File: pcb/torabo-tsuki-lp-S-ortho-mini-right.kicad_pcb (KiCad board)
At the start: 2 copper layers, 123.8 x 71.8 mm, 50 parts, among them J201 Conn_01x06_MountingPin, SW201 SW_SPDT, SW44 SW_Push, SW45 SW_Push, SW46 SW_Push, SW47 SW_Push, SW48 SW_Push, SW51 SW_Push, SW52 SW_Push, SW53 SW_Push, SW54 SW_Push, SW55 SW_Push, SW58 SW_Push, SW59 SW_Push, SW60 SW_Push, SW61 SW_Push, SW62 SW_Push, SW63 SW_Push, SW65 SW_Push, SW69 SW_Push, SW70 SW_Push, U201 BLEMicroPro

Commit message: Add outer key columns to split PCBs
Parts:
- added D43: D_Small, Library:D_SOD-123_HandSoldering, B.Cu at (157.3, 122.1)
- added D50: D_Small, Library:D_SOD-123_HandSoldering, B.Cu at (157.3, 139.1)
- added D57: D_Small, Library:D_SOD-123_HandSoldering, B.Cu at (157.3, 156.1)
- added D64: D_Small, Library:D_SOD-123_HandSoldering, B.Cu at (157.3, 173.1)
- added SW43: SW_Push, Library:CHOC_V2_SOCKET_HANDSOLDERING_17mm, B.Cu at (155.8, 126.0)
- added SW50: SW_Push, Library:CHOC_V2_SOCKET_HANDSOLDERING_17mm, B.Cu at (155.8, 143.0)
- added SW57: SW_Push, Library:CHOC_V2_SOCKET_HANDSOLDERING_17mm, B.Cu at (155.8, 160.0)
- added SW64: SW_Push, Library:CHOC_V2_SOCKET_HANDSOLDERING_17mm, B.Cu at (155.8, 177.0)
- moved REF** 17.0 mm to (164.3, 186.5)
- moved REF** 17.0 mm to (164.3, 116.5)
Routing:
- net /right/COL0: track 0.00 -> 169.3 mm, vias 0 -> 2
- net /right/ROW4: track 134.6 -> 153.2 mm, vias 4 -> 5
- net /right/ROW2: track 86.5 -> 105.1 mm, vias 5 -> 6
- net /right/ROW3: track 116.3 -> 134.9 mm, vias 6 -> 7
- net /right/ROW1: track 92.7 -> 111.3 mm, vias 5 -> 6
- net Net-(D43-K): track 0.00 -> 9.80 mm
- net Net-(D64-K): track 0.00 -> 9.80 mm
- net Net-(D57-K): track 0.00 -> 9.80 mm
- net Net-(D50-K): track 0.00 -> 9.80 mm
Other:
- board size 123.8 x 71.8 mm -> 140.8 x 71.8 mm

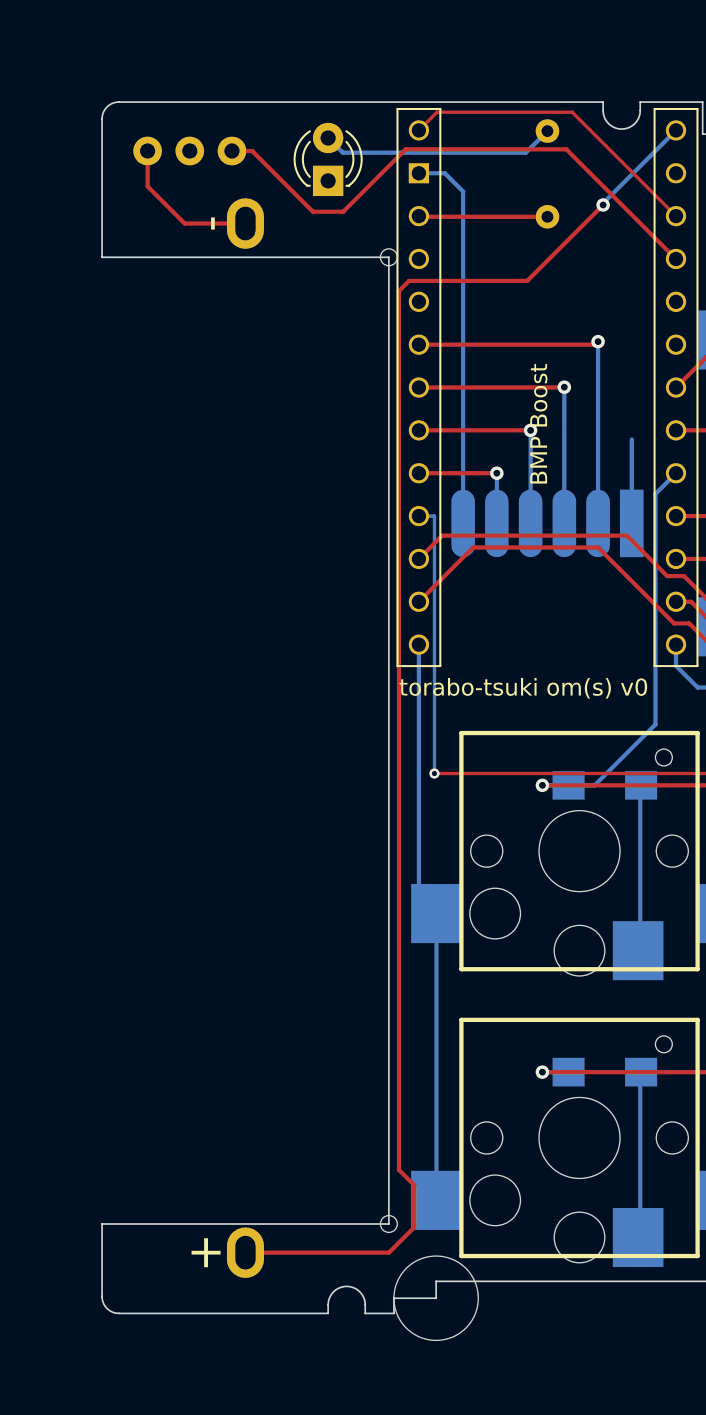
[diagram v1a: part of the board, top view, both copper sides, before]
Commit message: Adapt split keyboard PCBs for AAA battery holders
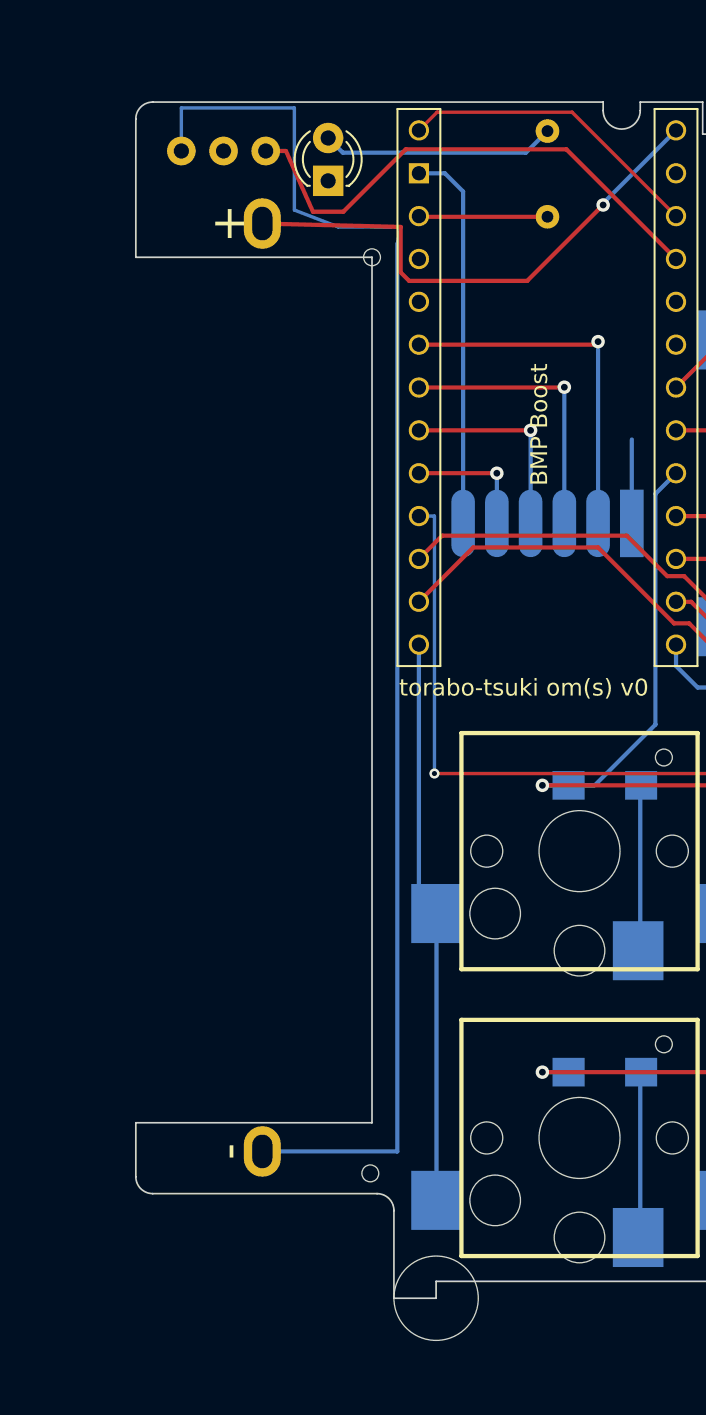
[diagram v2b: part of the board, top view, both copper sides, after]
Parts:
- BT201: value Battery_Cell -> Battery_Cell_AAA; footprint Library:battery_holder -> Library:battery_holder_AAA_1x_P55mm
- moved REF** 3.20 mm to (41.4, 179.1)
- moved BT201 3.16 mm to (35.0, 150.3), turned to 90 degrees
- moved SW201 2.00 mm to (32.7, 118.5)
- moved REF** 1.00 mm to (41.5, 124.8)
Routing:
- net Net-(BT201--): track 8.81 -> 84.6 mm
- net +BATT: track 86.9 -> 31.2 mm
- net /right/BOOT: track 32.0 -> 30.9 mm
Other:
- board size 140.8 x 71.8 mm -> 138.8 x 70.9 mm

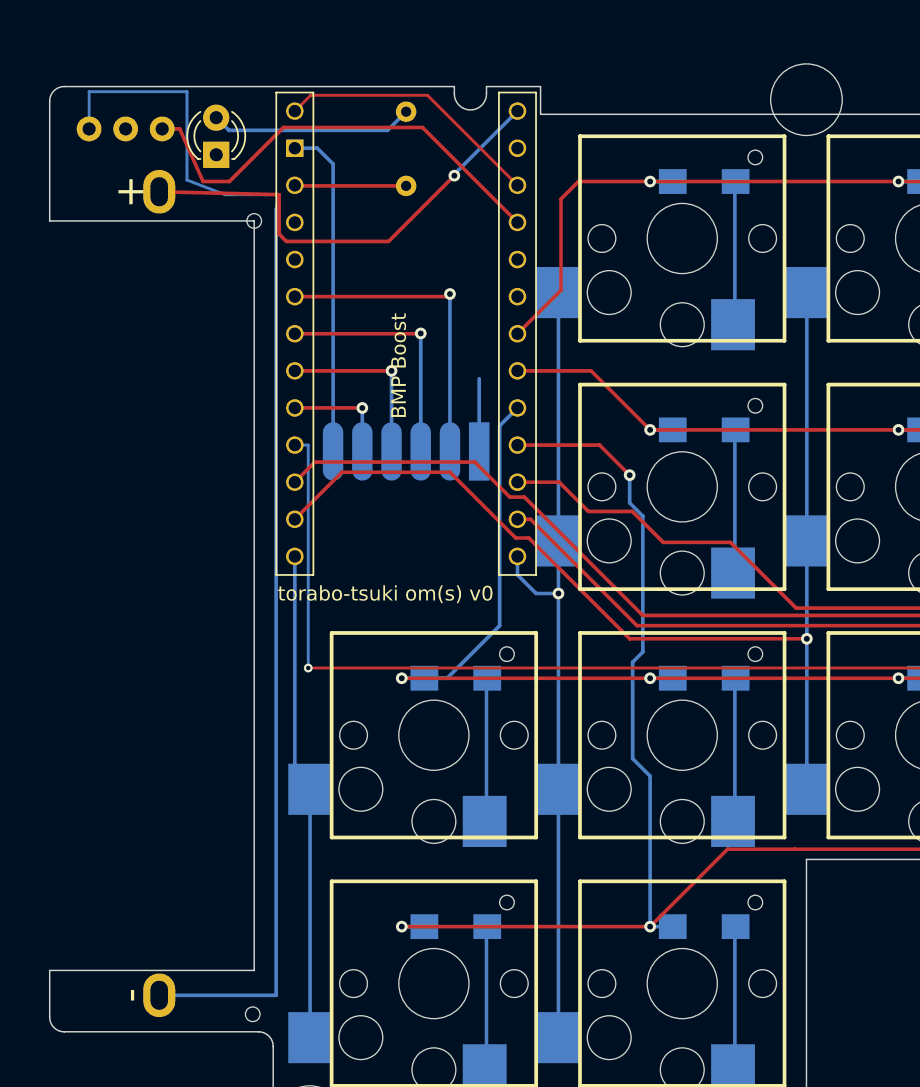
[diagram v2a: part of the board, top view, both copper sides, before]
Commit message: Migrate split PCBs to XIAO nRF52840 Plus
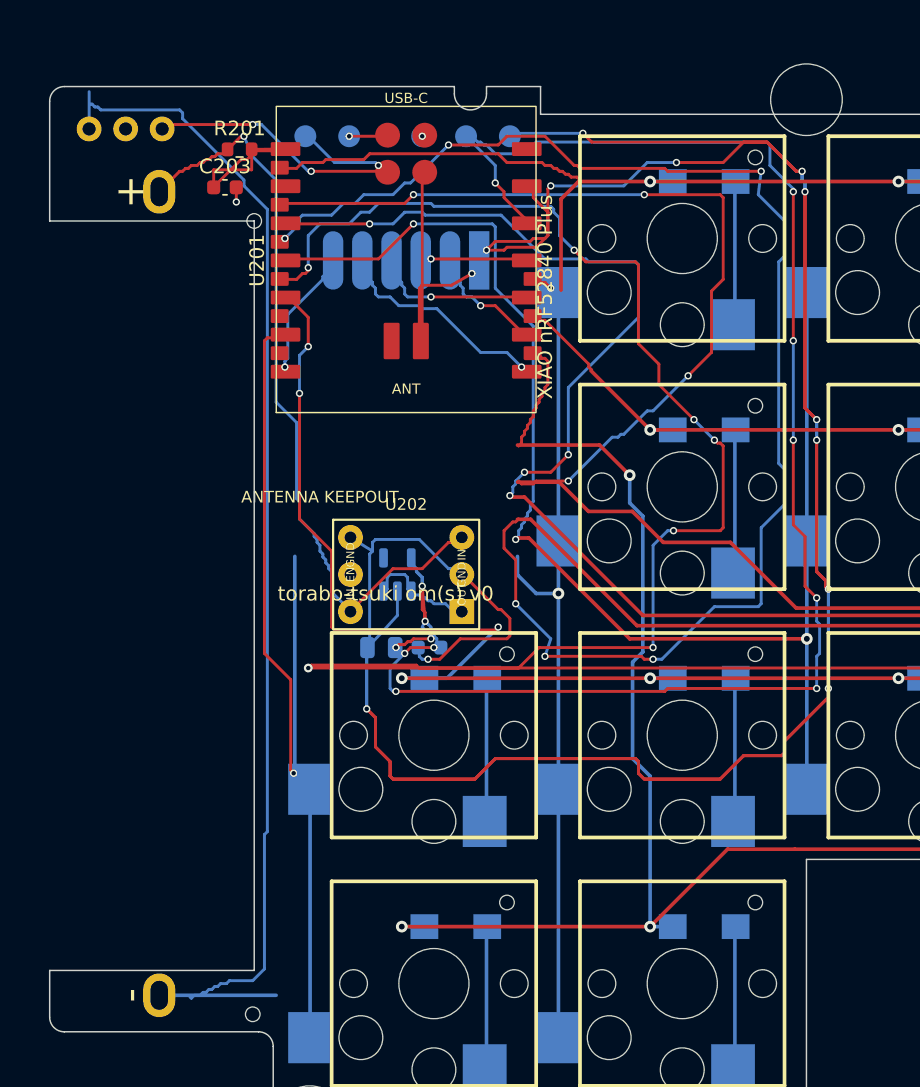
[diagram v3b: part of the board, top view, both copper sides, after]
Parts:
- removed D201: LED_Small, Library:LED_D3.0mm
- added C201: 10uF X7R, C_0805_2012Metric, B.Cu at (50.2, 154.0)
- added C202: 0.1uF X7R, C_0603_1608Metric, B.Cu at (53.5, 154.0)
- added C203: 0.1uF X7R, C_0603_1608Metric, F.Cu at (39.5, 122.5)
- added TP201: SWDIO, TestPoint_Pad_D1.5mm, B.Cu at (48.0, 119.0)
- added TP202: SWDCLK, TestPoint_Pad_D1.5mm, B.Cu at (53.0, 119.0)
- added TP203: RESET, TestPoint_Pad_D1.5mm, B.Cu at (45.0, 119.0)
- added TP204: 3V3, TestPoint_Pad_D1.5mm, B.Cu at (56.0, 119.0)
- added TP205: GND, TestPoint_Pad_D1.5mm, B.Cu at (59.0, 119.0)
- added U202: AE-XCL103-3V3, AE-XCL103-3V3, F.Cu at (51.9, 149.0)
- added U203: XC8111AA01MR-G, SOT-23-5, B.Cu at (51.3, 149.0)
- R201: value 330 -> 10k; footprint Library:R_Axial_DIN0204_L3.6mm_D1.6mm_P5.08mm_Horizontal -> R_0603_1608Metric; moved to F.Cu
- U201: value BLEMicroPro -> XIAO nRF52840 Plus; footprint Library:BLEMicroPro -> XIAO-nRF52840-Plus-SMD
- moved J201 13.1 mm to (51.9, 127.5)
- moved R201 11.7 mm to (40.5, 119.9), turned to 0 degrees
- moved U201 10.2 mm to (51.9, 127.5), turned to 90 degrees
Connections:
- R201 pad 1: /right/LED -> +BATT
- R201 pad 2: Net-(D201-A) -> /right/VBAT_ADC
- SW201 pad 3: /right/BOOT -> /right/RESET_N
- U201 pad 1: GND -> /right/VBAT_ADC
- U201 pad 10: /right/COL0 -> /right/MOTION
- U201 pad 11: /right/COL2 -> /right/SDIO
- U201 pad 12: /right/COL4 -> /right/SYS_3V3
- U201 pad 13: /right/COL6 -> GND
- U201 pad 14: /right/COL5 -> (no net)
- U201 pad 15: /right/COL3 -> /right/ROW1
- U201 pad 17: /right/ROW4 -> /right/COL3
- U201 pad 18: /right/ROW3 -> /right/COL0
- U201 pad 19: /right/ROW2 -> (no net)
- U201 pad 2: VCC -> /right/ROW0
- U201 pad 20: /right/ROW1 -> (no net)
- U201 pad 21: /right/ROW0 -> /right/ROW4
- U201 pad 22: unconnected-(U201-4V3-Pad22) -> /right/ROW2
- U201 pad 23: /right/BOOT -> /right/COL5
- U201 pad 24: GND -> /right/SWDIO
- U201 pad 25: unconnected-(U201-+5V-Pad25) -> /right/SWDCLK
- U201 pad 26: +BATT -> /right/RESET_N
- U201 pad 3: /right/LED -> /right/COL2
- U201 pad 4: GND -> /right/COL4
- U201 pad 5: unconnected-(U201-GND-Pad5) -> /right/ROW3
- U201 pad 6: /right/SCLK -> /right/COL6
- U201 pad 7: /right/SDIO -> VCC
- U201 pad 8: /right/MOTION -> /right/CS
- U201 pad 9: /right/CS -> /right/SCLK
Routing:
- net GND: track 23.2 -> 276.7 mm, vias 0 -> 14
- net /right/SYS_3V3: track 0.00 -> 119.2 mm, vias 0 -> 13
- net /right/COL3: track 73.8 -> 170.3 mm, vias 1 -> 7
- net /right/COL0: track 169.3 -> 241.1 mm, vias 2 -> 8
- net /right/COL1: track 125.4 -> 184.3 mm, vias 1 -> 5
- net /right/COL6: track 33.4 -> 65.5 mm, vias 0 -> 1
- net /right/BOOT: track 30.9 -> 0.00 mm
- net /right/COL2: track 108.2 -> 138.6 mm, vias 1 -> 5
- net /right/RESET_N: track 0.00 -> 23.7 mm, vias 0 -> 3
- net +BATT: track 31.2 -> 53.4 mm
- net /right/ROW3: track 134.9 -> 155.8 mm, vias 7 -> 10
- net /right/COL4: track 75.1 -> 95.4 mm, vias 1 -> 3
- net /right/ROW1: track 111.3 -> 129.0 mm
- net /right/VBAT_ADC: track 0.00 -> 14.2 mm
- net Net-(D201-A): track 13.9 -> 0.00 mm
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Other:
- board text added: "ANTENNA KEEPOUT"
- board text added: "XIAO nRF52840 Plus"
- board text removed: "BMP Boost"

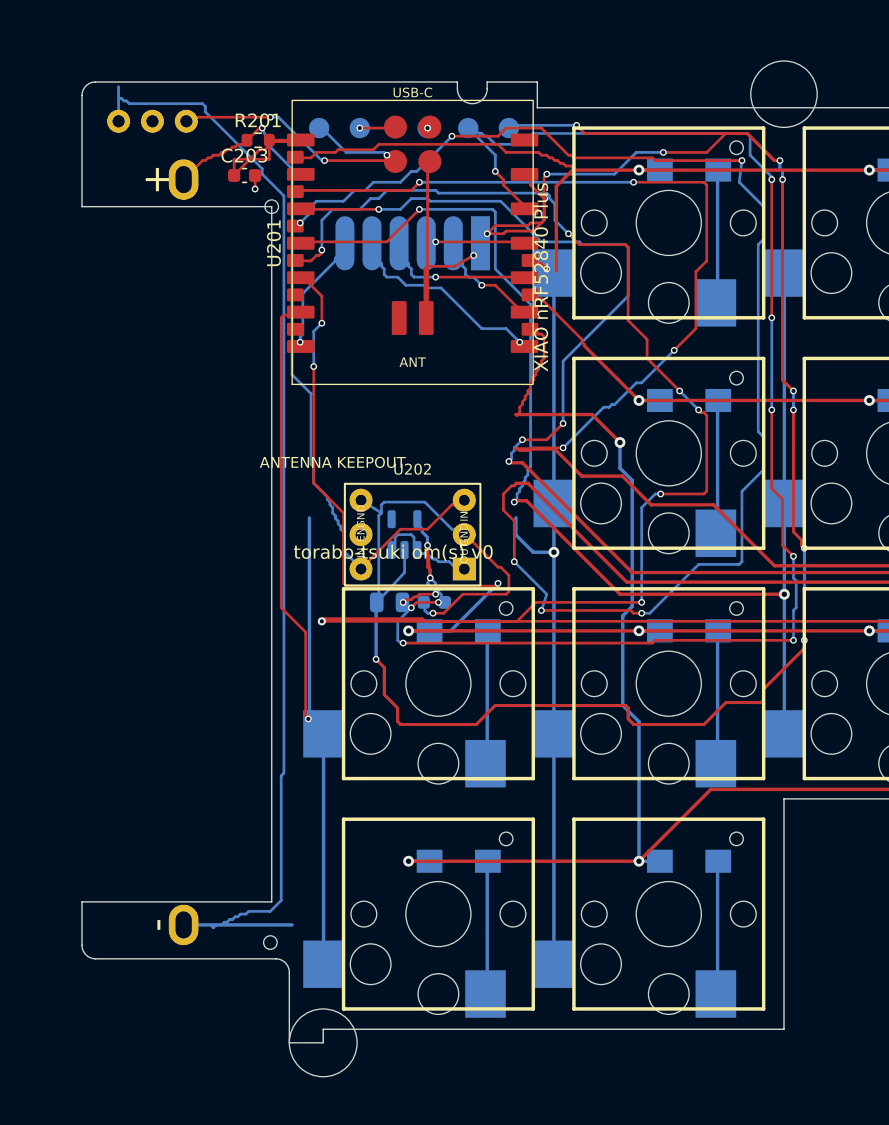
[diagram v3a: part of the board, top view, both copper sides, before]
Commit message: Compact XIAO and battery PCB layout
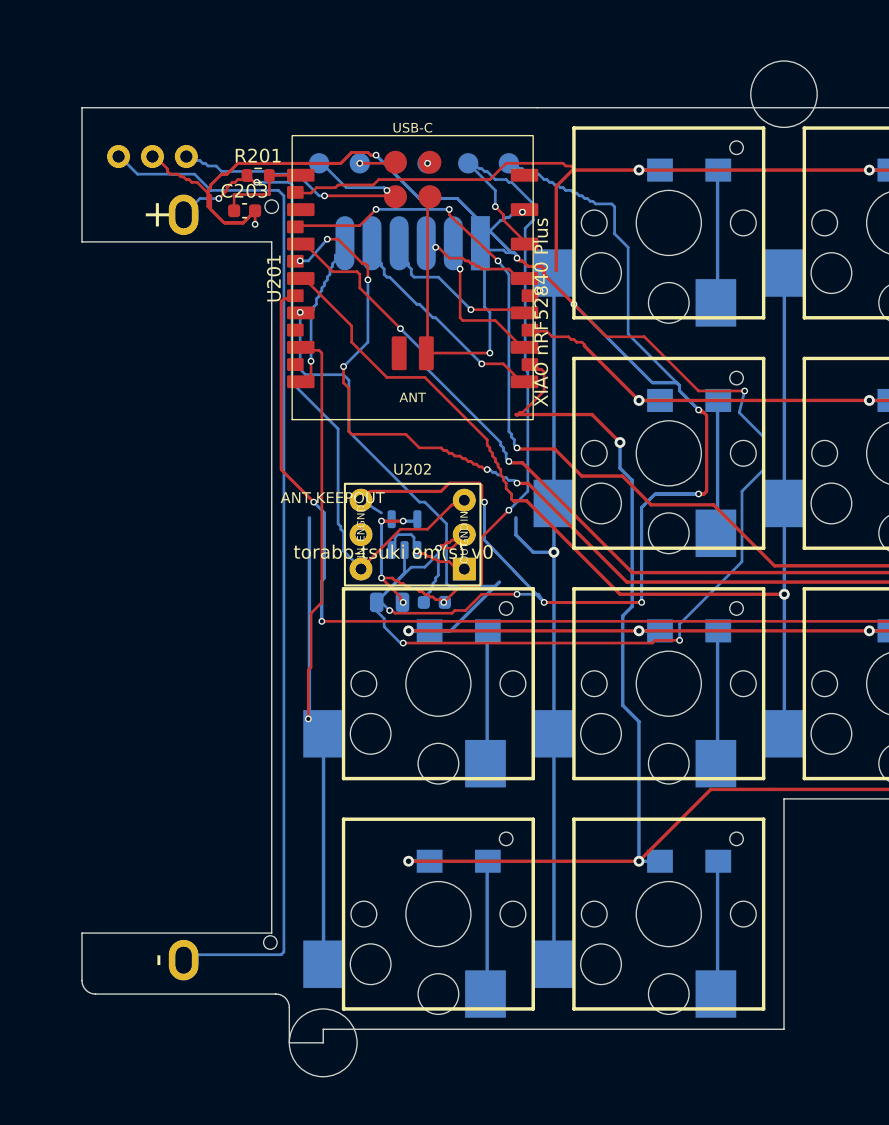
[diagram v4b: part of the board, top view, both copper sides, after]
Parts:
- moved BT201 2.60 mm to (35.0, 152.9)
- moved C203 2.60 mm to (39.5, 125.1)
- moved R201 2.60 mm to (40.5, 122.5)
- moved SW201 2.60 mm to (32.7, 121.1)
- moved TP201 2.60 mm to (48.0, 121.6)
- moved TP202 2.60 mm to (53.0, 121.6)
- moved TP203 2.60 mm to (45.0, 121.6)
- moved TP204 2.60 mm to (56.0, 121.6)
- moved TP205 2.60 mm to (59.0, 121.6)
- moved U201 2.60 mm to (51.9, 130.1)
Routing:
- net GND: track 276.7 -> 394.9 mm, vias 14 -> 17
- net /right/COL3: track 170.3 -> 108.0 mm
- net /right/SYS_3V3: track 119.2 -> 68.9 mm, vias 13 -> 7
- net /right/COL0: track 241.1 -> 205.6 mm, vias 8 -> 3
- net /right/COL1: track 184.3 -> 157.2 mm
- net /right/COL2: track 138.6 -> 115.7 mm, vias 5 -> 3
- net /right/COL4: track 95.4 -> 81.9 mm, vias 3 -> 1
- net Net-(BT201--): track 84.1 -> 77.0 mm
- net /right/VBAT_ADC: track 14.2 -> 7.52 mm
- net /right/ROW3: track 155.8 -> 150.0 mm, vias 10 -> 8
- net /right/SCLK: track 8.28 -> 11.5 mm
- net +BATT: track 53.4 -> 50.5 mm, vias 1 -> 2
- net /right/COL6: track 65.5 -> 62.7 mm
- net VCC: track 9.36 -> 12.1 mm
- net /right/ROW4: track 161.2 -> 158.7 mm
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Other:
- board size 138.8 x 70.9 mm -> 138.8 x 69 mm
- board text added: "ANT KEEPOUT"
- board text removed: "ANTENNA KEEPOUT"
